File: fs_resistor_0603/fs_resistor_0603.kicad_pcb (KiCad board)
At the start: 2 copper layers, 3 parts

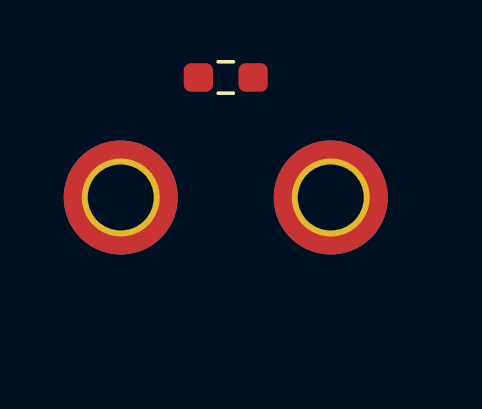
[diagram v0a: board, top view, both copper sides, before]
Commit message: resistor 0603 stitch breakout board
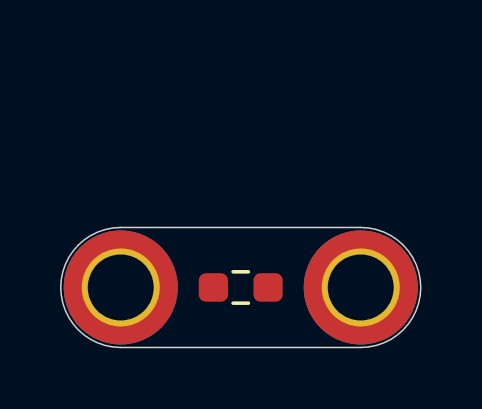
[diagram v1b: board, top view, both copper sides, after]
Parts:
- moved R1 7.02 mm to (149.0, 83.0)
- moved H2 3.16 mm to (153.0, 83.0)
- moved H1 3.00 mm to (145.0, 83.0)
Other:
- board outline added: 12 x 4 mm
- board text added: "0603"
- board text added: "@flicker stitch"
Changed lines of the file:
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@@
 	(footprint "MountingHole:MountingHole_2.2mm_M2_DIN965_Pad_TopBottom"
 		(layer "F.Cu")
-		(at 152 80)
+		(at 153 83)
 		(descr "Mounting Hole 2.2mm, M2, generated by kicad-footprint-generator mountinghole.py")
 		(tags "mountinghole M2 DIN965")
@@
 	(footprint "Resistor_SMD:R_0603_1608Metric_Pad0.98x0.95mm_HandSolder"
 		(layer "F.Cu")
-		(at 148.5 76)
+		(at 149 83)
 		(descr "Resistor SMD 0603 (1608 Metric), square (rectangular) end terminal, IPC-7351 nominal with elongated pad for handsoldering. (Body size source: IPC-SM-782 page 72, https://www.pcb-3d.com/wordpress/wp-content/uploads/ipc-sm-782a_amendment_1_and_2.pdf)")
 		(tags "resistor handsolder")
@@
 	(footprint "MountingHole:MountingHole_2.2mm_M2_DIN965_Pad_TopBottom"
 		(layer "F.Cu")
-		(at 145 80)
+		(at 145 83)
 		(descr "Mounting Hole 2.2mm, M2, generated by kicad-footprint-generator mountinghole.py")
 		(tags "mountinghole M2 DIN965")
@@
 		(embedded_fonts no)
 	)
+	(gr_line
+		(start 145 81)
+		(end 153 81)
+		(stroke
+			(width 0.05)
+			(type default)
+		)
+		(layer "Edge.Cuts")
+	)
+	(gr_arc
+		(start 145 85)
+		(mid 143 83)
+		(end 145 81)
+		(stroke
+			(width 0.05)
+			(type default)
+		)
+		(layer "Edge.Cuts")
+	)
+	(gr_line
+		(start 145 85)
+		(end 153 85)
+		(stroke
+			(width 0.05)
+			(type default)
+		)
+		(layer "Edge.Cuts")
+	)
+	(gr_arc
+		(start 153 81)
+		(mid 155 83)
+		(end 153 85)
+		(stroke
+			(width 0.05)
+			(type default)
+		)
+		(layer "Edge.Cuts")
+	)
+	(gr_text "@flicker\nstitch"
+		(at 149 85 0)
+		(layer "B.SilkS")
+		(effects
+			(font
+				(size 0.7 0.7)
+			)
+			(justify bottom mirror)
+		)
+	)
+	(gr_text "0603"
+		(at 149 82.35 0)
+		(layer "B.SilkS")
+		(effects
+			(font
+				(size 1 1)
+				(thickness 0.1)
+			)
+			(justify bottom mirror)
+		)
+	)
 	(embedded_fonts no)

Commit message: add plus sign on resistor boards
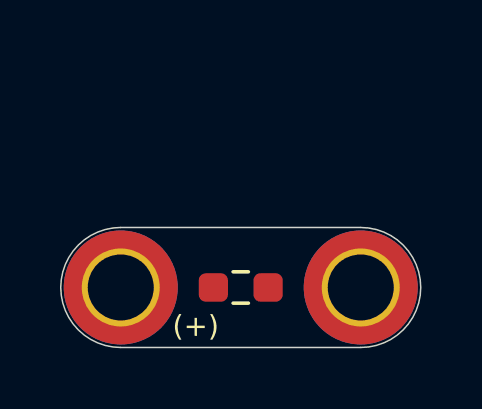
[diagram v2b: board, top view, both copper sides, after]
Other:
- board text added: "(+)"
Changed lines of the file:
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@@
 		(layer "Edge.Cuts")
+	)
+	(gr_text "(+)"
+		(at 147.5 84.7 0)
+		(layer "F.SilkS")
+		(effects
+			(font
+				(size 0.7 0.7)
+			)
+			(justify bottom)
+		)
 	)
 	(gr_text "@flicker\nstitch"

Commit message: resistor 0603 order
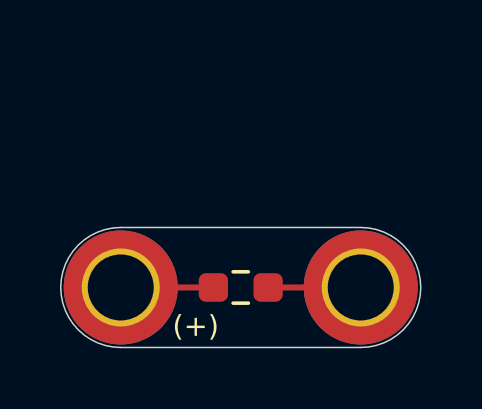
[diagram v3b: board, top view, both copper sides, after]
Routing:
- net Net-(H2-Pad1): track 0.00 -> 3.09 mm
- net Net-(H1-Pad1): track 0.00 -> 3.09 mm
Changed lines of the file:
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@@
 		)
+	)
+	(segment
+		(start 149.9125 83)
+		(end 153 83)
+		(width 0.2)
+		(layer "F.Cu")
+		(net "Net-(H2-Pad1)")
+	)
+	(segment
+		(start 148.0875 83)
+		(end 145 83)
+		(width 0.2)
+		(layer "F.Cu")
+		(net "Net-(H1-Pad1)")
 	)
 	(embedded_fonts no)
